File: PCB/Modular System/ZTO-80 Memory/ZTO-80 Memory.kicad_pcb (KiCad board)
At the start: 2 copper layers, 99.1 x 57.1 mm, 12 parts, among them J1 ZTO-80 Bus, J2 Conn_01x02, U1 28C256, U2 AS6C62256, U3 74HC139

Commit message: Edited power LED resistor value
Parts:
- R1: value 200 -> 220

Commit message: Updates to PDFs and the SBC
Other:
- board text added: "ZTO-80 MEMORY"
- board text added: "v1.1"
- board text removed: "BACK"
- board text removed: "ZTO-80 MEMORY V1.1"
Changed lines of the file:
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@@
-(kicad_pcb (version 20171130) (host pcbnew "(5.1.6)-1")
+(kicad_pcb (version 20171130) (host pcbnew "(5.1.5)-3")
   (general
     (thickness 1.6)
@@
     )
   )
-  (gr_text "ZTO-80 MEMORY V1.1" (at 145.415 109.22) (layer F.SilkS)
+  (gr_text v1.1 (at 172.085 115.57) (layer F.SilkS)
+    (effects (font (size 1.524 1.524) (thickness 0.2032)) (justify left))
+  )
+  (gr_text "ZTO-80 MEMORY" (at 145.415 109.855) (layer F.SilkS)
     (effects (font (size 2.54 2.54) (thickness 0.254)))
   )
@@
     (effects (font (size 1.27 1.27) (thickness 0.15)))
   )
-  (gr_text BACK (at 193.04 91.44 90) (layer B.SilkS)
-    (effects (font (size 2.032 2.032) (thickness 0.2032)) (justify mirror))
-  )
   (gr_text JLCJLCJLCJLC (at 189.865 118.745) (layer B.SilkS)

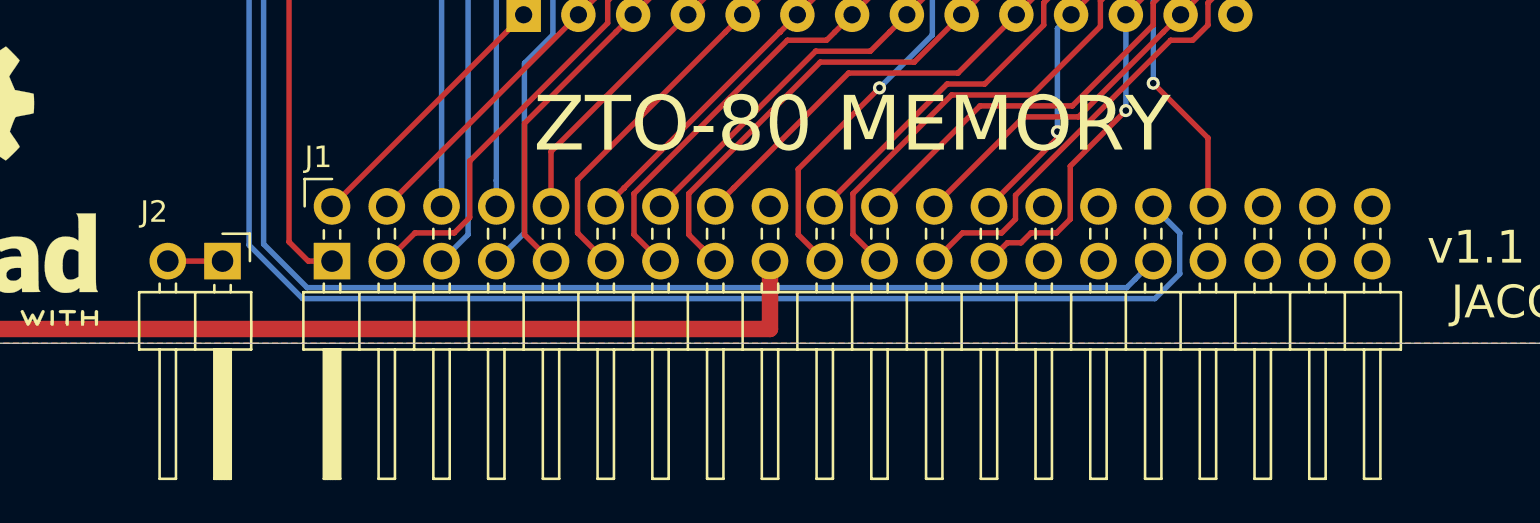
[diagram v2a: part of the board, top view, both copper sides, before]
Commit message: Changed bus orientation
This change is backwards-compatible with all previous ZTO-80 modules
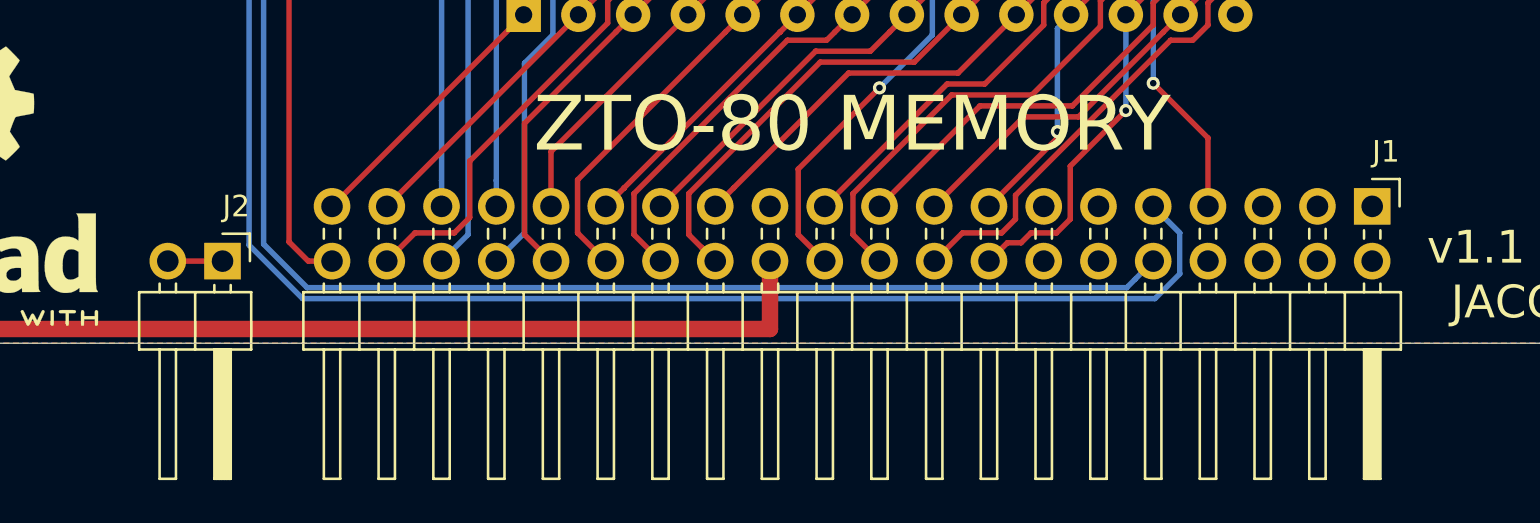
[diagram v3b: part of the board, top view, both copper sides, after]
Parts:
- J1: footprint ZTO-80_Header:PinHeader_2x20_P2.54mm_Horizontal -> Connector_PinHeader_2.54mm:PinHeader_2x20_P2.54mm_Horizontal
- moved J1 48.3 mm to (169.5, 113.7), turned to 270 degrees
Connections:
- J1 pad 1: /A15 -> /USR4
- J1 pad 10: /A6 -> /MREQ
- J1 pad 11: /A5 -> /INT
- J1 pad 12: /A4 -> /RST
- J1 pad 13: /A3 -> /M1
- J1 pad 14: /A2 -> /CLK
- J1 pad 15: /A1 -> /D0
- J1 pad 16: /A0 -> /D1
- J1 pad 17: VCC -> /D2
- J1 pad 18: GND -> /D3
- J1 pad 19: /D7 -> /D4
- J1 pad 2: /A14 -> /USR3
- J1 pad 20: /D6 -> /D5
- J1 pad 21: /D5 -> /D6
- J1 pad 22: /D4 -> /D7
- J1 pad 23: /D3 -> GND
- J1 pad 24: /D2 -> VCC
- J1 pad 25: /D1 -> /A0
- J1 pad 26: /D0 -> /A1
- J1 pad 27: /CLK -> /A2
- J1 pad 28: /M1 -> /A3
- J1 pad 29: /RST -> /A4
- J1 pad 3: /A13 -> /USR2
- J1 pad 30: /INT -> /A5
- J1 pad 31: /MREQ -> /A6
- J1 pad 32: /WR -> /A7
- J1 pad 33: /IORQ -> /A8
- J1 pad 34: /RD -> /A9
- J1 pad 35: /TXB -> /A10
- J1 pad 36: /RXB -> /A11
- J1 pad 37: /USR1 -> /A12
- J1 pad 38: /USR2 -> /A13
- J1 pad 39: /USR3 -> /A14
- J1 pad 4: /A12 -> /USR1
- J1 pad 40: /USR4 -> /A15
- J1 pad 5: /A11 -> /RXB
- J1 pad 6: /A10 -> /TXB
- J1 pad 7: /A9 -> /RD
- J1 pad 8: /A8 -> /IORQ
- J1 pad 9: /A7 -> /WR

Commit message: Added CERN license text to silkscreen
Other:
- board text added: "Licensed under CERN-OHL-S v2"
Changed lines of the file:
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@@
   (general
     (thickness 1.6)
-    (drawings 15)
+    (drawings 16)
     (tracks 301)
     (zones 0)
@@
     )
   )
+  (gr_text "Licensed under CERN-OHL-S v2" (at 109.22 118.745) (layer B.SilkS)
+    (effects (font (size 1 1) (thickness 0.15)) (justify mirror))
+  )
   (gr_text v1.1 (at 172.085 115.57) (layer F.SilkS)

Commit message: Finished Memory
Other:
- board text added: "28C256"
- board text added: "74HC139"
- board text added: "AS6C62256"
